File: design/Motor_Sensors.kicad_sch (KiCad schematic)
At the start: 7 parts, among them J5 HALL_ENC, SW1 SENSOR_VOLTAGE

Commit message: Agregue LCSC Part # a algunas resistencias
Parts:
- R34, R35, R36: LCSC (none) -> C227479
- R37: LCSC (none) -> C98220
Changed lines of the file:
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@@
+			)
+		)
+		(property "LCSC" "C98220"
+			(at 177.8 78.74 0)
+			(effects
+				(font
+					(size 1.27 1.27)
+				)
+				(hide yes)
 			)
 		)
@@
 			)
 		)
+		(property "LCSC" "C227479"
+			(at 143.51 80.01 0)
+			(effects
+				(font
+					(size 1.27 1.27)
+				)
+				(hide yes)
+			)
+		)
 		(pin "1"
 		)
@@
 		)
 		(property "MPN" "AC0603DR-072K2L"
+			(at 134.62 77.47 0)
+			(effects
+				(font
+					(size 1.27 1.27)
+				)
+				(hide yes)
+			)
+		)
+		(property "LCSC" "C227479"
 			(at 134.62 77.47 0)
 			(effects
@@
 			(at 153.67 82.55 0)
 			(effects
+				(font
+					(size 1.27 1.27)
+				)
+				(hide yes)
+			)
+		)
+		(property "LCSC" "C227479"
+			(at 153.67 82.55 0)
+			(effects

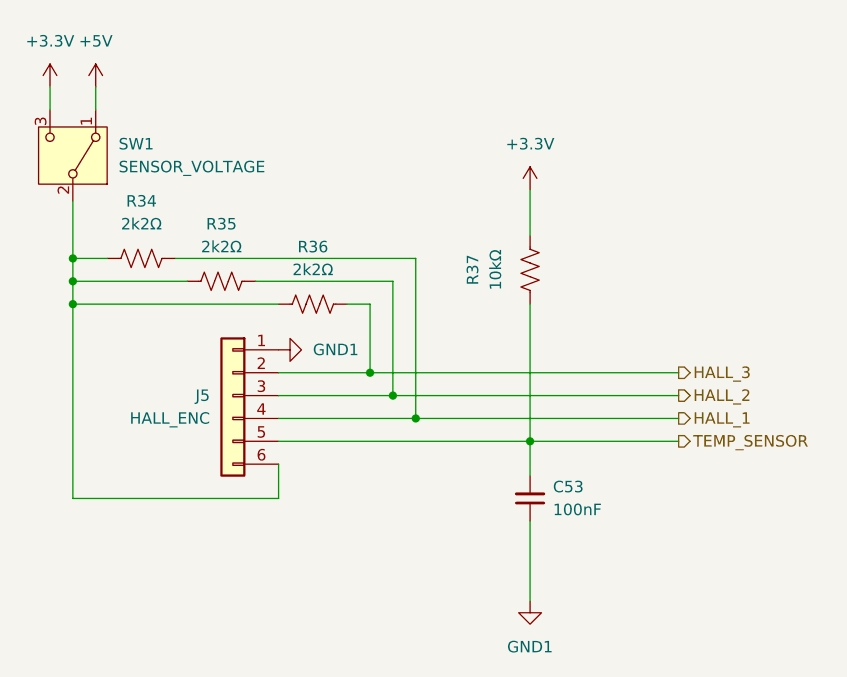
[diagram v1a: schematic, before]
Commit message: Cambio de switch de tension del sensor por jumper
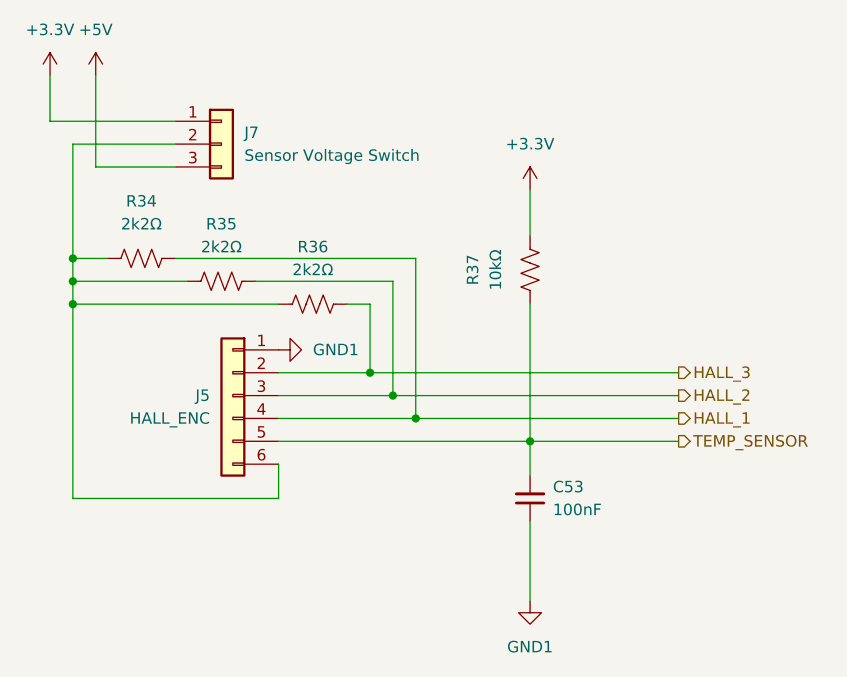
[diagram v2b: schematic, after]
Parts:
- removed SW1: SENSOR_VOLTAGE, Button_Switch_THT:SW_Slide-03_Wuerth-WS-SLTV_10x2.5x6.4_P2.54mm, symbol Switch:SW_SPDT
- added J7: Sensor Voltage Switch, Connector_PinHeader_2.54mm:PinHeader_1x03_P2.54mm_Vertical, symbol Connector_Generic:Conn_01x03
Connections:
- net +3.3V: now also J7.1 (Pin_1)
- net +5V: now also J7.3 (Pin_3)
- net at J5.6 (Pin_6), R34.2, R35.2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: now also J7.2 (Pin_2)
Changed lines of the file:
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@@
+	(wire
+		(pts
+			(xy 138.43 67.31) (xy 129.54 67.31)
+		)
+		(stroke
+			(width 0)
+			(type default)
+		)
+	)
 	(wire
 		(pts
@@
 	(wire
 		(pts
+			(xy 138.43 62.23) (xy 124.46 62.23)
+		)
+		(stroke
+			(width 0)
+			(type default)
+		)
+	)
+	(wire
+		(pts
 			(xy 127 80.01) (xy 127 77.47)
 		)
@@
 	(wire
 		(pts
-			(xy 129.54 60.96) (xy 129.54 58.42)
+			(xy 129.54 57.15) (xy 129.54 67.31)
 		)
 		(stroke
@@
 	(wire
 		(pts
+			(xy 138.43 64.77) (xy 127 64.77)
+		)
+		(stroke
+			(width 0)
+			(type default)
+		)
+	)
+	(wire
+		(pts
 			(xy 130.81 77.47) (xy 127 77.47)
 		)
@@
 	(wire
 		(pts
-			(xy 127 71.12) (xy 127 77.47)
+			(xy 127 64.77) (xy 127 77.47)
 		)
 		(stroke
@@
 	(wire
 		(pts
-			(xy 124.46 60.96) (xy 124.46 58.42)
+			(xy 124.46 57.15) (xy 124.46 62.23)
 		)
 		(stroke
@@
 	(symbol
 		(lib_id "power:+3.3V")
-		(at 124.46 58.42 0)
+		(at 124.46 57.15 0)
 		(unit 1)
 		(exclude_from_sim no)
@@
 		(fields_autoplaced yes)
 		(property "Reference" "#PWR067"
-			(at 124.46 62.23 0)
+			(at 124.46 60.96 0)
 			(effects
 				(font
@@
 		)
 		(property "Value" "+3.3V"
-			(at 124.46 53.34 0)
+			(at 124.46 52.07 0)
 			(effects
 				(font
@@
 		)
 		(property "Footprint" ""
-			(at 124.46 58.42 0)
+			(at 124.46 57.15 0)
 			(effects
 				(font
@@
 		)
 		(property "Datasheet" ""
-			(at 124.46 58.42 0)
+			(at 124.46 57.15 0)
 			(effects
 				(font
@@
 		)
 		(property "Description" "Power symbol creates a global label with name \"+3.3V\""
-			(at 124.46 58.42 0)
+			(at 124.46 57.15 0)
 			(effects
 				(font
@@
 				(path "/6389d757-a1bd-4c0a-9d55-6114b19cc67a/b1ebc81e-c8d0-4dfc-b018-5639ecb79376"
 					(reference "#PWR067")
+					(unit 1)
+				)
+			)
+		)
+	)
+	(symbol
+		(lib_id "Connector_Generic:Conn_01x03")
+		(at 143.51 64.77 0)
+		(unit 1)
+		(exclude_from_sim no)
+		(in_bom yes)
+		(on_board yes)
+		(dnp no)
+		(fields_autoplaced yes)
+		(property "Reference" "J7"
+			(at 146.05 63.4999 0)
+			(effects
+				(font
+					(size 1.27 1.27)
+				)
+				(justify left)
+			)
+		)
+		(property "Value" "Sensor Voltage Switch"
+			(at 146.05 66.0399 0)
+			(effects
+				(font
+					(size 1.27 1.27)
+				)
+				(justify left)
+			)
+		)
+		(property "Footprint" "Connector_PinHeader_2.54mm:PinHeader_1x03_P2.54mm_Vertical"
+			(at 143.51 64.77 0)
+			(effects
+				(font
+					(size 1.27 1.27)
+				)
+				(hide yes)
+			)
+		)
+		(property "Datasheet" "~"
+			(at 143.51 64.77 0)
+			(effects
+				(font
+					(size 1.27 1.27)
+				)
+				(hide yes)
+			)
+		)
+		(property "Description" "Generic connector, single row, 01x03, script generated (kicad-library-utils/schlib/autogen/connector/)"
+			(at 143.51 64.77 0)
+			(effects
+				(font
+					(size 1.27 1.27)
+				)
+				(hide yes)
+			)
+		)
+		(property "LCSC" "C2937625"
+			(at 143.51 64.77 0)
+			(effects
+				(font
+					(size 1.27 1.27)
+				)
+				(hide yes)
+			)
+		)
+		(property "MPN" "PZ254V-11-03P"
+			(at 143.51 64.77 0)
+			(effects
+				(font
+					(size 1.27 1.27)
+				)
+				(hide yes)
+			)
+		)
+		(property "Manufacturer" "XFCN"
+			(at 143.51 64.77 0)
+			(effects
+				(font
+					(size 1.27 1.27)
+				)
+				(hide yes)
+			)
+		)
+		(pin "1"
+		)
+		(pin "3"
+		)
+		(pin "2"
+		)
+		(instances
+			(project ""
+				(path "/6389d757-a1bd-4c0a-9d55-6114b19cc67a/b1ebc81e-c8d0-4dfc-b018-5639ecb79376"
+					(reference "J7")
 					(unit 1)
 				)
@@
 				(path "/6389d757-a1bd-4c0a-9d55-6114b19cc67a/b1ebc81e-c8d0-4dfc-b018-5639ecb79376"
 					(reference "C53")
-					(unit 1)
-				)
-			)
-		)
-	)
-	(symbol
-		(lib_id "Switch:SW_SPDT")
-		(at 127 66.04 270)
-		(mirror x)
-		(unit 1)
-		(exclude_from_sim no)
-		(in_bom yes)
-		(on_board yes)
-		(dnp no)
-		(fields_autoplaced yes)
-		(property "Reference" "SW1"
-			(at 132.08 64.7699 90)
-			(effects
-				(font
-					(size 1.27 1.27)
-				)
-				(justify left)
-			)
-		)
-		(property "Value" "SENSOR_VOLTAGE"
-			(at 132.08 67.3099 90)
-			(effects
-				(font
-					(size 1.27 1.27)
-				)
-				(justify left)
-			)
-		)
-		(property "Footprint" "Button_Switch_THT:SW_Slide-03_Wuerth-WS-SLTV_10x2.5x6.4_P2.54mm"
-			(at 127 66.04 0)
-			(effects
-				(font
-					(size 1.27 1.27)
-				)
-				(hide yes)
-			)
-		)
-		(property "Datasheet" ""
-			(at 127 66.04 0)
-			(effects
-				(font
-					(size 1.27 1.27)
-				)
-				(hide yes)
-			)
-		)
-		(property "Description" "SWITCH SLIDE SPDT 500MA 12V"
-			(at 127 66.04 0)
-			(effects
-				(font
-					(size 1.27 1.27)
-				)
-				(hide yes)
-			)
-		)
-		(property "Manufacturer" "Würth Elektronik"
-			(at 127 66.04 90)
-			(effects
-				(font
-					(size 1.27 1.27)
-				)
-				(hide yes)
-			)
-		)
-		(property "MPN" "450301014042"
-			(at 127 66.04 0)
-			(effects
-				(font
-					(size 1.27 1.27)
-				)
-				(hide yes)
-			)
-		)
-		(pin "3"
-		)
-		(pin "2"
-		)
-		(pin "1"
-		)
-		(instances
-			(project "ESCX"
-				(path "/6389d757-a1bd-4c0a-9d55-6114b19cc67a/b1ebc81e-c8d0-4dfc-b018-5639ecb79376"
-					(reference "SW1")
 					(unit 1)
 				)
@@
 	(symbol
 		(lib_id "power:+5V")
-		(at 129.54 58.42 0)
+		(at 129.54 57.15 0)
 		(unit 1)
 		(exclude_from_sim no)
@@
 		(fields_autoplaced yes)
 		(property "Reference" "#PWR068"
-			(at 129.54 62.23 0)
+			(at 129.54 60.96 0)
 			(effects
 				(font
@@
 		)
 		(property "Value" "+5V"
-			(at 129.54 53.34 0)
+			(at 129.54 52.07 0)
 			(effects
 				(font
@@
 		)
 		(property "Footprint" ""
-			(at 129.54 58.42 0)
+			(at 129.54 57.15 0)
 			(effects
 				(font
@@
 		)
 		(property "Datasheet" ""
-			(at 129.54 58.42 0)
+			(at 129.54 57.15 0)
 			(effects
 				(font
@@
 		)
 		(property "Description" "Power symbol creates a global label with name \"+5V\""
-			(at 129.54 58.42 0)
-			(effects
-				(font
+			(at 129.54 57.15 0)
+			(effects
+				(font

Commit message: Abaratando costos
Cambios en numeros de jlcpcb, pasados a componentes básicos
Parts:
- J5, J7: now left out of the parts list
- R34, R35, R36: LCSC C227479 -> C4190
- R37: LCSC C98220 -> C25804
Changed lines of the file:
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@@
 			)
 		)
-		(property "LCSC" "C98220"
+		(property "LCSC" "C25804"
 			(at 177.8 78.74 0)
 			(effects
@@
 		(unit 1)
 		(exclude_from_sim no)
-		(in_bom yes)
+		(in_bom no)
 		(on_board yes)
 		(dnp no)
@@
 		)
 		(instances
-			(project ""
+			(project "ESCX"
 				(path "/6389d757-a1bd-4c0a-9d55-6114b19cc67a/b1ebc81e-c8d0-4dfc-b018-5639ecb79376"
 					(reference "J7")
@@
 			)
 		)
-		(property "LCSC" "C227479"
+		(property "LCSC" "C4190"
 			(at 143.51 80.01 0)
 			(effects
@@
 			)
 		)
-		(property "LCSC" "C227479"
+		(property "LCSC" "C4190"
 			(at 134.62 77.47 0)
 			(effects
@@
 		(unit 1)
 		(exclude_from_sim no)
-		(in_bom yes)
+		(in_bom no)
 		(on_board yes)
 		(dnp no)
@@
 			)
 		)
-		(property "LCSC" "C227479"
+		(property "LCSC" "C4190"
 			(at 153.67 82.55 0)
 			(effects

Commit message: Guardado esquemático
Faltó guardar
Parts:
- J5: footprint Connector_JST:JST_XH_B6B-XH-AM_1x06_P2.50mm_Vertical -> Connector_PinSocket_2.54mm:PinSocket_1x06_P2.54mm_Vertical
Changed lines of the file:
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@@
 			)
 		)
-		(property "Footprint" "Connector_JST:JST_XH_B6B-XH-AM_1x06_P2.50mm_Vertical"
+		(property "Footprint" "Connector_PinSocket_2.54mm:PinSocket_1x06_P2.54mm_Vertical"
 			(at 144.78 92.71 0)
 			(effects

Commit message: Cambios
Actualizado footprint de USB, cambio de capacitor de feedback por uno básico, pequeños cambios en la ubicación de los footprints.
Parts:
- C53: MPN CC0603KRX7R9BB104 -> (none); Manufacturer YAGEO -> (none)
- J5: MPN B6B-XH-A -> (none); Manufacturer JST -> (none)
- J7: MPN PZ254V-11-03P -> (none); Manufacturer XFCN -> (none)
- R34, R35, R36: MPN AC0603DR-072K2L -> (none); Manufacturer YAGEO -> (none)
- R37: MPN RC0603FR-0710KL -> (none); Manufacturer YAGEO -> (none)
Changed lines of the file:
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@@
-			)
-		)
-		(property "Manufacturer" "YAGEO"
-			(at 177.8 78.74 0)
-			(effects
-				(font
-					(size 1.27 1.27)
-				)
-				(hide yes)
-			)
-		)
-		(property "MPN" "RC0603FR-0710KL"
-			(at 177.8 78.74 0)
-			(effects
-				(font
-					(size 1.27 1.27)
-				)
-				(hide yes)
 			)
 		)
@@
 			)
 		)
-		(property "MPN" "PZ254V-11-03P"
-			(at 143.51 64.77 0)
-			(effects
-				(font
-					(size 1.27 1.27)
-				)
-				(hide yes)
-			)
-		)
-		(property "Manufacturer" "XFCN"
-			(at 143.51 64.77 0)
-			(effects
-				(font
-					(size 1.27 1.27)
-				)
-				(hide yes)
-			)
-		)
 		(pin "1"
 		)
@@
 			)
 		)
-		(property "Manufacturer" "YAGEO"
-			(at 143.51 80.01 0)
-			(effects
-				(font
-					(size 1.27 1.27)
-				)
-				(hide yes)
-			)
-		)
-		(property "MPN" "AC0603DR-072K2L"
-			(at 143.51 80.01 0)
-			(effects
-				(font
-					(size 1.27 1.27)
-				)
-				(hide yes)
-			)
-		)
 		(property "LCSC" "C4190"
 			(at 143.51 80.01 0)
@@
 			)
 		)
-		(property "Manufacturer" "YAGEO"
-			(at 134.62 77.47 0)
-			(effects
-				(font
-					(size 1.27 1.27)
-				)
-				(hide yes)
-			)
-		)
-		(property "MPN" "AC0603DR-072K2L"
-			(at 134.62 77.47 0)
-			(effects
-				(font
-					(size 1.27 1.27)
-				)
-				(hide yes)
-			)
-		)
 		(property "LCSC" "C4190"
 			(at 134.62 77.47 0)
@@
 		)
 		(property "Description" "CAP 100n, 50V, 0603"
-			(at 177.8 104.14 0)
-			(effects
-				(font
-					(size 1.27 1.27)
-				)
-				(hide yes)
-			)
-		)
-		(property "Manufacturer" "YAGEO"
-			(at 177.8 104.14 0)
-			(effects
-				(font
-					(size 1.27 1.27)
-				)
-				(hide yes)
-			)
-		)
-		(property "MPN" "CC0603KRX7R9BB104"
 			(at 177.8 104.14 0)
 			(effects
@@
 			)
 		)
-		(property "Manufacturer" "JST"
-			(at 144.78 92.71 0)
-			(effects
-				(font
-					(size 1.27 1.27)
-				)
-				(hide yes)
-			)
-		)
-		(property "MPN" "B6B-XH-A"
-			(at 144.78 92.71 0)
-			(effects
-				(font
-					(size 1.27 1.27)
-				)
-				(hide yes)
-			)
-		)
 		(property "LCSC" "C144397"
 			(at 142.24 92.7099 0)
@@
 			(at 153.67 82.55 0)
 			(effects
-				(font
-					(size 1.27 1.27)
-				)
-				(hide yes)
-			)
-		)
-		(property "Manufacturer" "YAGEO"
-			(at 153.67 82.55 0)
-			(effects
-				(font
-					(size 1.27 1.27)
-				)
-				(hide yes)
-			)
-		)
-		(property "MPN" "AC0603DR-072K2L"
-			(at 153.67 82.55 0)
-			(effects
